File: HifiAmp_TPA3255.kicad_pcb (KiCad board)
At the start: 4 copper layers, 200 x 150 mm, 124 parts, among them J1 PVDD 48V IN — NEEDS_DATA, J2 RCA L SE, J3 RCA R SE, J301 SPK_L, J302 SPK_R, J4 VOLUME_REMOTE, Q301 IPP330P10NM, Q302 IXTK200N10L2, U1 LM5010ASD, U2 LM2940IMP-12/NOPB, U3 TLV1117-33IDCY, U4 OPA1612AIDR, U5 OPA1612AIDR, U6 TPA3255B, U7 TPS3802K33DCKR, U8 LM5069-2

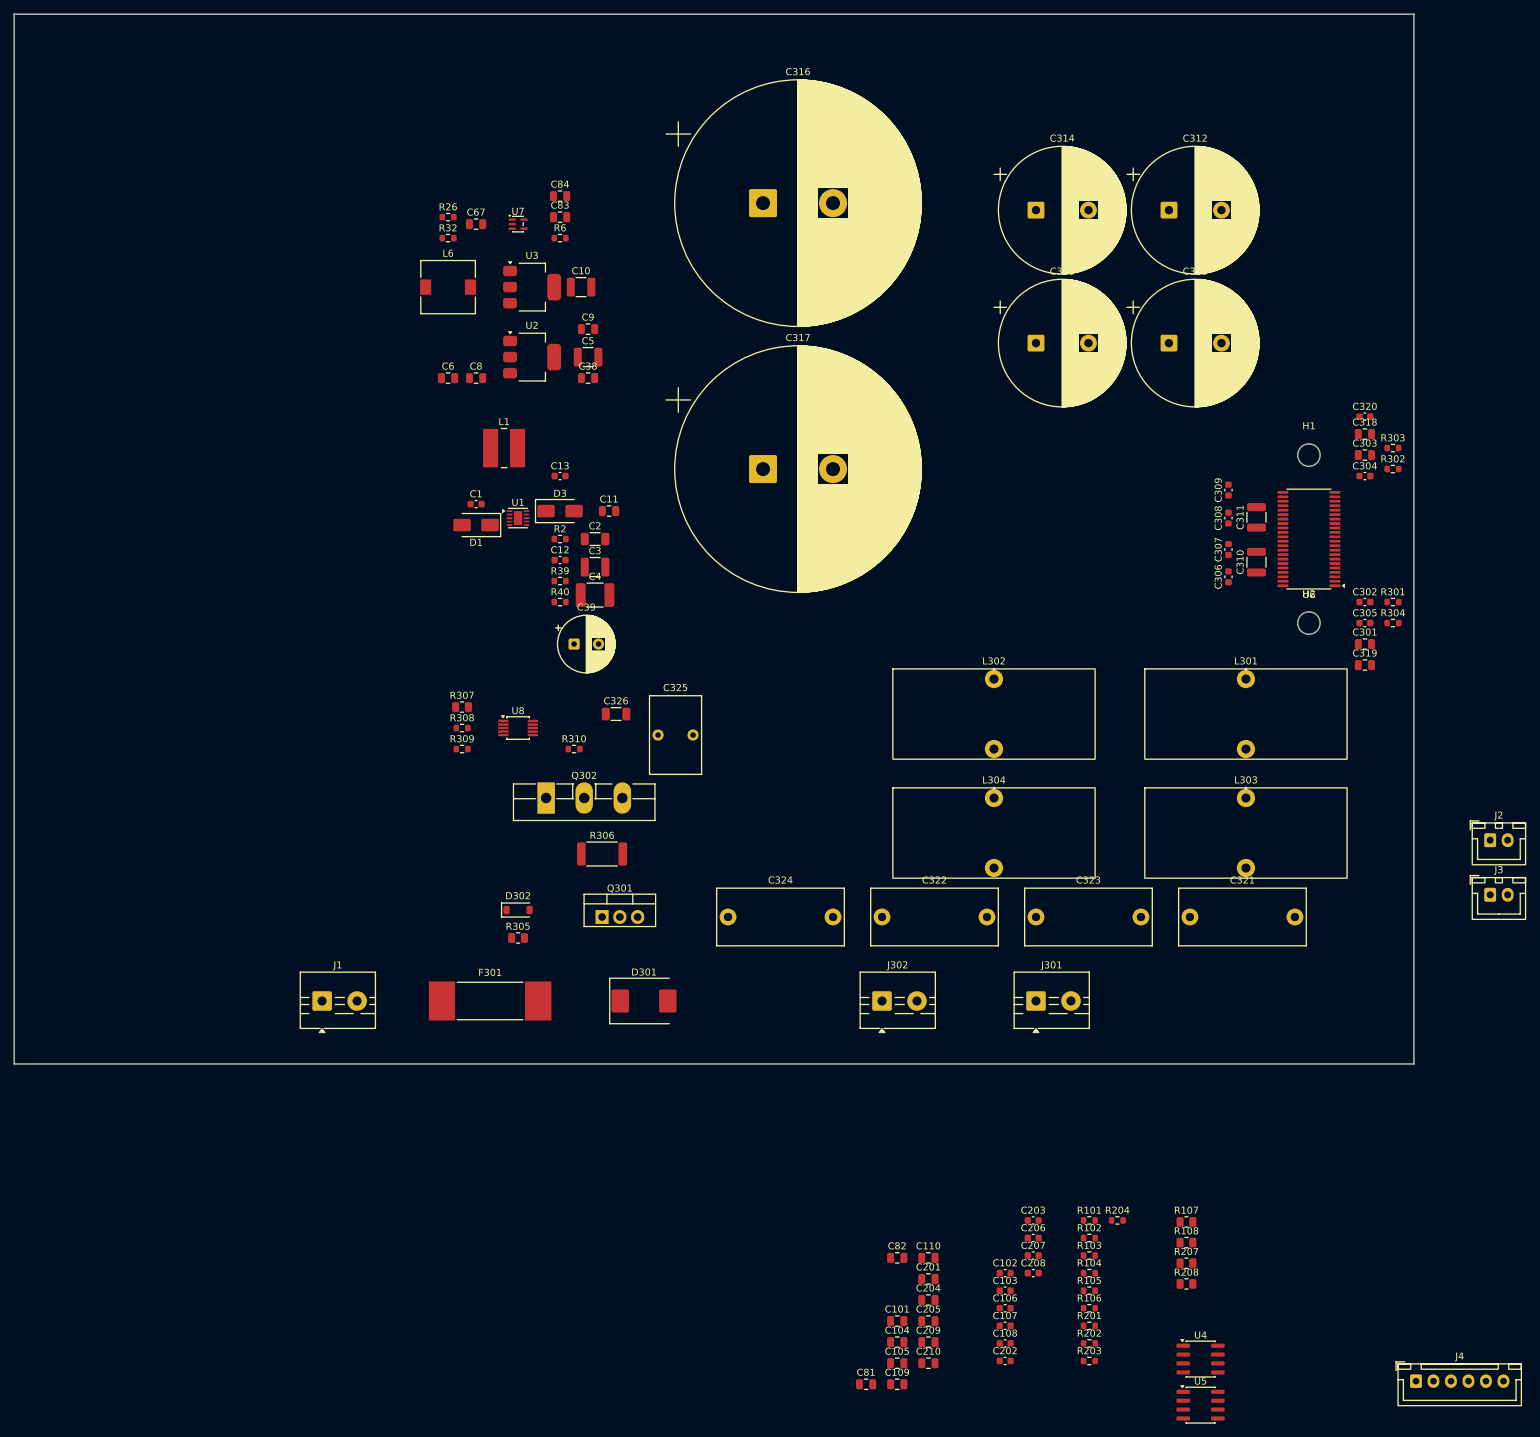
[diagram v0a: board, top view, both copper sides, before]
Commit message: feat(e1.4): let the OPA1612's own pinout lay out the left channel
U4 turns single-ended into differential: amplifier A takes the SOIC-8's left
flank — pad 1 the output, pad 2 the inverting input, pad 3 VMID, pad 4 GND —
and amplifier B the right flank, re-inverting A's output to make the opposite
phase. So each feedback network stays on its own amplifier's side, R102/C102
left between pads 1 and 2, R104/C103 right between pads 7 and 6. Only R103
crosses the package, because it is the part that carries A's output to B's
input; that traverse is the topology, not a placement mistake.

C110 sits against U4 rather than between the channels. Splitting VMID into
C110 and C210 was decided precisely so each op-amp gets its own, and centring
one of them would undo that.

The twenty footprints stay inside x 100..155, the band held clear for low-level
analog at the edge opposite U6 since E1.3. J2's pad 1 is the footprint origin,
so at x = 104 the connector grows away from the board edge and keeps 2 mm to
it, against a 0.5 mm rule.

Proven: DRC 101 violations, every one silkscreen; no clearance, no
courtyards_overlap, lib_footprint_mismatch still 0. pad_prop_heatsink still
present exactly once — the E1.10 regression did not come back on this move,
which is the thing worth watching each time an IC is placed. schematic_parity
0, 254 unconnected unchanged, 124 footprints, the 83 earlier placements intact
to the micron. 103 of 124 placed.

Co-Authored-By: Claude Opus 5 <noreply@anthropic.com>
Claude-Session: https://claude.ai/code/session_013Xf3ag9SHfw8Y4oCwQtx85
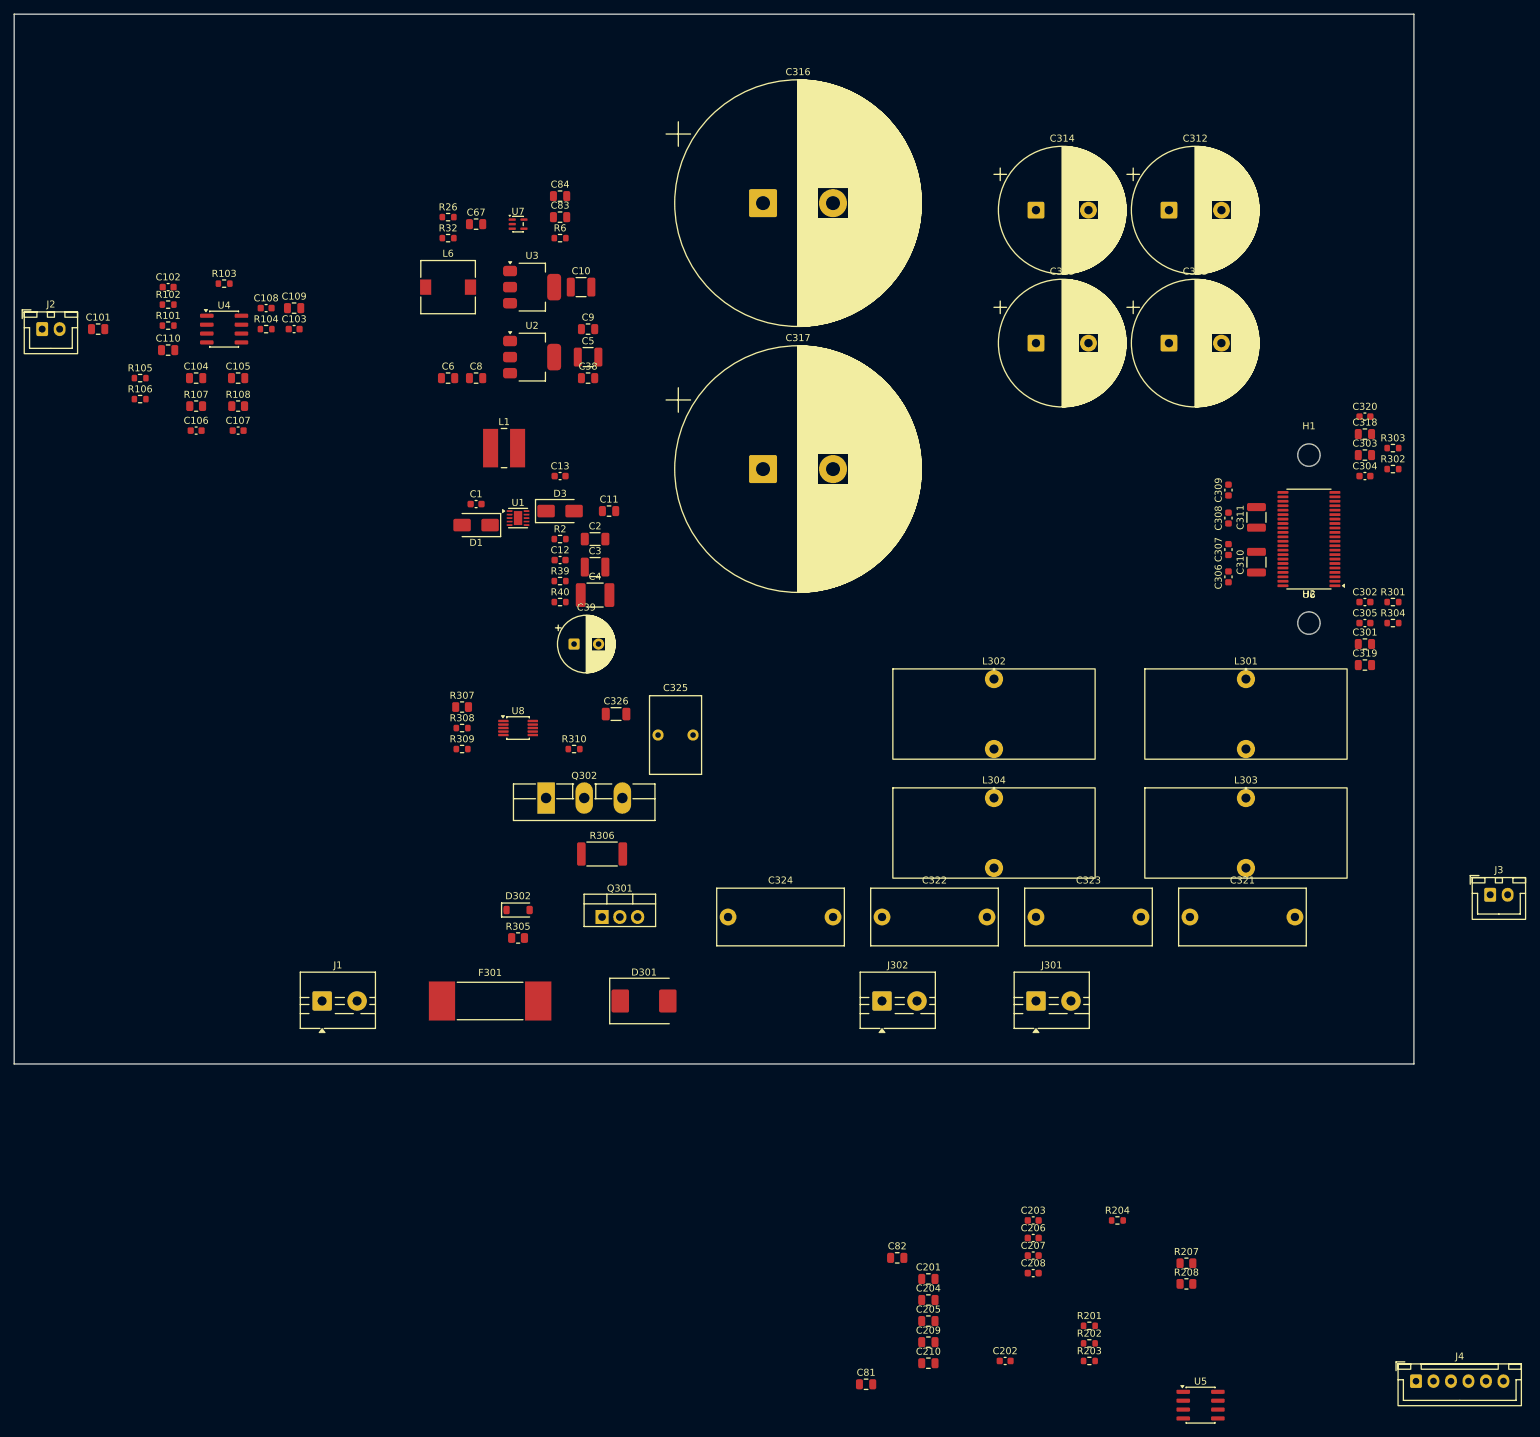
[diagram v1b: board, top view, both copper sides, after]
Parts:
- moved J2 219.4 mm to (104.0, 145.0)
- moved U4 202.8 mm to (130.0, 145.0)
- moved R105 188.1 mm to (118.0, 152.0)
- moved R106 187.8 mm to (118.0, 155.0)
- moved R102 187.4 mm to (122.0, 141.5)
- moved R103 185.9 mm to (130.0, 138.5)
- moved C102 184.8 mm to (122.0, 139.0)
- moved R101 183.5 mm to (122.0, 144.5)
- moved R107 183.3 mm to (126.0, 156.0)
- moved C101 182.0 mm to (112.0, 145.0)
- moved C108 181.7 mm to (136.0, 142.0)
- moved R108 180.7 mm to (132.0, 156.0)
- moved R104 179.0 mm to (136.0, 145.0)
- moved C109 176.3 mm to (140.0, 142.0)
- moved C103 170.9 mm to (140.0, 145.0)
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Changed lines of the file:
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@@
 	(footprint "Capacitor_SMD:C_0805_2012Metric"
 		(layer "F.Cu")
-		(at 230.625 277.705)
+		(at 122 148)
 		(descr "Capacitor SMD 0805 (2012 Metric), square (rectangular) end terminal, IPC-7351 nominal, (Body size source: IPC-SM-782 page 76, https://www.pcb-3d.com/wordpress/wp-content/uploads/ipc-sm-782a_amendment_1_and_2.pdf, https://docs.google.com/spreadsheets/d/1BsfQQcO9C6DZCsRaXUlFlo91Tg2WpOkGARC1WS5S8t0/edit?usp=sharing)")
 		(tags "capacitor")
@@
 	(footprint "Capacitor_SMD:C_0805_2012Metric"
 		(layer "F.Cu")
-		(at 226.175 286.735)
+		(at 112 145)
 		(descr "Capacitor SMD 0805 (2012 Metric), square (rectangular) end terminal, IPC-7351 nominal, (Body size source: IPC-SM-782 page 76, https://www.pcb-3d.com/wordpress/wp-content/uploads/ipc-sm-782a_amendment_1_and_2.pdf, https://docs.google.com/spreadsheets/d/1BsfQQcO9C6DZCsRaXUlFlo91Tg2WpOkGARC1WS5S8t0/edit?usp=sharing)")
 		(tags "capacitor")
@@
 	(footprint "Resistor_SMD:R_0603_1608Metric"
 		(layer "F.Cu")
-		(at 253.625 272.355)
+		(at 122 144.5)
 		(descr "Resistor SMD 0603 (1608 Metric), square (rectangular) end terminal, IPC-7351 nominal, (Body size source: IPC-SM-782 page 72, https://www.pcb-3d.com/wordpress/wp-content/uploads/ipc-sm-782a_amendment_1_and_2.pdf)")
 		(tags "resistor")
@@
 	(footprint "Resistor_SMD:R_0603_1608Metric"
 		(layer "F.Cu")
-		(at 253.625 277.375)
+		(at 130 138.5)
 		(descr "Resistor SMD 0603 (1608 Metric), square (rectangular) end terminal, IPC-7351 nominal, (Body size source: IPC-SM-782 page 72, https://www.pcb-3d.com/wordpress/wp-content/uploads/ipc-sm-782a_amendment_1_and_2.pdf)")
 		(tags "resistor")
@@
 	(footprint "Capacitor_SMD:C_0805_2012Metric"
 		(layer "F.Cu")
-		(at 226.175 292.755)
+		(at 132 152)
 		(descr "Capacitor SMD 0805 (2012 Metric), square (rectangular) end terminal, IPC-7351 nominal, (Body size source: IPC-SM-782 page 76, https://www.pcb-3d.com/wordpress/wp-content/uploads/ipc-sm-782a_amendment_1_and_2.pdf, https://docs.google.com/spreadsheets/d/1BsfQQcO9C6DZCsRaXUlFlo91Tg2WpOkGARC1WS5S8t0/edit?usp=sharing)")
 		(tags "capacitor")
@@
 	(footprint "Capacitor_SMD:C_0805_2012Metric"
 		(layer "F.Cu")
-		(at 226.175 289.745)
+		(at 126 152)
 		(descr "Capacitor SMD 0805 (2012 Metric), square (rectangular) end terminal, IPC-7351 nominal, (Body size source: IPC-SM-782 page 76, https://www.pcb-3d.com/wordpress/wp-content/uploads/ipc-sm-782a_amendment_1_and_2.pdf, https://docs.google.com/spreadsheets/d/1BsfQQcO9C6DZCsRaXUlFlo91Tg2WpOkGARC1WS5S8t0/edit?usp=sharing)")
 		(tags "capacitor")
@@
 	(footprint "Resistor_SMD:R_0603_1608Metric"
 		(layer "F.Cu")
-		(at 253.625 284.905)
+		(at 118 155)
 		(descr "Resistor SMD 0603 (1608 Metric), square (rectangular) end terminal, IPC-7351 nominal, (Body size source: IPC-SM-782 page 72, https://www.pcb-3d.com/wordpress/wp-content/uploads/ipc-sm-782a_amendment_1_and_2.pdf)")
 		(tags "resistor")
@@
 	(footprint "Capacitor_SMD:C_0603_1608Metric"
 		(layer "F.Cu")
-		(at 241.595 284.905)
+		(at 126 159.5)
 		(descr "Capacitor SMD 0603 (1608 Metric), square (rectangular) end terminal, IPC-7351 nominal, (Body size source: IPC-SM-782 page 76, https://www.pcb-3d.com/wordpress/wp-content/uploads/ipc-sm-782a_amendment_1_and_2.pdf)")
 		(tags "capacitor")
@@
 	(footprint "Package_SO:SOIC-8_3.9x4.9mm_P1.27mm"
 		(layer "F.Cu")
-		(at 269.515 292.16)
+		(at 130 145)
 		(descr "SOIC, 8 Pin (JEDEC MS-012AA, https://www.analog.com/media/en/package-pcb-resources/package/pkg_pdf/soic_narrow-r/r_8.pdf)")
 		(tags "SOIC SO")
@@
 	(footprint "Resistor_SMD:R_0805_2012Metric"
 		(layer "F.Cu")
-		(at 267.495 272.575)
+		(at 126 156)
 		(descr "Resistor SMD 0805 (2012 Metric), square (rectangular) end terminal, IPC-7351 nominal, (Body size source: IPC-SM-782 page 72, https://www.pcb-3d.com/wordpress/wp-content/uploads/ipc-sm-782a_amendment_1_and_2.pdf)")
 		(tags "resistor")
@@
 	(footprint "Connector_JST:JST_XH_B2B-XH-A_1x02_P2.50mm_Vertical"
 		(layer "F.Cu")
-		(at 310.895 218.025)
+		(at 104 145)
 		(descr "JST XH series connector, B2B-XH-A (http://www.jst-mfg.com/product/pdf/eng/eXH.pdf)")
 		(tags "connector JST XH vertical")
@@
 	(footprint "Capacitor_SMD:C_0603_1608Metric"
 		(layer "F.Cu")
-		(at 241.595 279.885)
+		(at 122 139)
 		(descr "Capacitor SMD 0603 (1608 Metric), square (rectangular) end terminal, IPC-7351 nominal, (Body size source: IPC-SM-782 page 76, https://www.pcb-3d.com/wordpress/wp-content/uploads/ipc-sm-782a_amendment_1_and_2.pdf)")
 		(tags "capacitor")
@@
 	(footprint "Capacitor_SMD:C_0603_1608Metric"
 		(layer "F.Cu")
-		(at 241.595 289.925)
+		(at 136 142)
 		(descr "Capacitor SMD 0603 (1608 Metric), square (rectangular) end terminal, IPC-7351 nominal, (Body size source: IPC-SM-782 page 76, https://www.pcb-3d.com/wordpress/wp-content/uploads/ipc-sm-782a_amendment_1_and_2.pdf)")
 		(tags "capacitor")
@@
 	(footprint "Resistor_SMD:R_0603_1608Metric"
 		(layer "F.Cu")
-		(at 253.625 282.395)
+		(at 118 152)
 		(descr "Resistor SMD 0603 (1608 Metric), square (rectangular) end terminal, IPC-7351 nominal, (Body size source: IPC-SM-782 page 72, https://www.pcb-3d.com/wordpress/wp-content/uploads/ipc-sm-782a_amendment_1_and_2.pdf)")
 		(tags "resistor")
@@
 	(footprint "Resistor_SMD:R_0805_2012Metric"
 		(layer "F.Cu")
-		(at 267.495 275.525)
+		(at 132 156)
 		(descr "Resistor SMD 0805 (2012 Metric), square (rectangular) end terminal, IPC-7351 nominal, (Body size source: IPC-SM-782 page 72, https://www.pcb-3d.com/wordpress/wp-content/uploads/ipc-sm-782a_amendment_1_and_2.pdf)")
 		(tags "resistor")
@@
 	(footprint "Resistor_SMD:R_0603_1608Metric"
 		(layer "F.Cu")
-		(at 253.625 274.865)
+		(at 122 141.5)
 		(descr "Resistor SMD 0603 (1608 Metric), square (rectangular) end terminal, IPC-7351 nominal, (Body size source: IPC-SM-782 page 72, https://www.pcb-3d.com/wordpress/wp-content/uploads/ipc-sm-782a_amendment_1_and_2.pdf)")
 		(tags "resistor")
@@
 	(footprint "Resistor_SMD:R_0603_1608Metric"
 		(layer "F.Cu")
-		(at 253.625 279.885)
+		(at 136 145)
 		(descr "Resistor SMD 0603 (1608 Metric), square (rectangular) end terminal, IPC-7351 nominal, (Body size source: IPC-SM-782 page 72, https://www.pcb-3d.com/wordpress/wp-content/uploads/ipc-sm-782a_amendment_1_and_2.pdf)")
 		(tags "resistor")
@@
 	(footprint "Capacitor_SMD:C_0603_1608Metric"
 		(layer "F.Cu")
-		(at 241.595 287.415)
+		(at 132 159.5)
 		(descr "Capacitor SMD 0603 (1608 Metric), square (rectangular) end terminal, IPC-7351 nominal, (Body size source: IPC-SM-782 page 76, https://www.pcb-3d.com/wordpress/wp-content/uploads/ipc-sm-782a_amendment_1_and_2.pdf)")
 		(tags "capacitor")
@@
 	(footprint "Capacitor_SMD:C_0603_1608Metric"
 		(layer "F.Cu")
-		(at 241.595 282.395)
+		(at 140 145)
 		(descr "Capacitor SMD 0603 (1608 Metric), square (rectangular) end terminal, IPC-7351 nominal, (Body size source: IPC-SM-782 page 76, https://www.pcb-3d.com/wordpress/wp-content/uploads/ipc-sm-782a_amendment_1_and_2.pdf)")
 		(tags "capacitor")
@@
 	(footprint "Capacitor_SMD:C_0805_2012Metric"
 		(layer "F.Cu")
-		(at 226.175 295.765)
+		(at 140 142)
 		(descr "Capacitor SMD 0805 (2012 Metric), square (rectangular) end terminal, IPC-7351 nominal, (Body size source: IPC-SM-782 page 76, https://www.pcb-3d.com/wordpress/wp-content/uploads/ipc-sm-782a_amendment_1_and_2.pdf, https://docs.google.com/spreadsheets/d/1BsfQQcO9C6DZCsRaXUlFlo91Tg2WpOkGARC1WS5S8t0/edit?usp=sharing)")
 		(tags "capacitor")
